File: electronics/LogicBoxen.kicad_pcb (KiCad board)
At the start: 2 copper layers, 50 x 35 mm, 47 parts, among them P1 Input, P2 Output, P3 Power, P4 L2, P5 L1, P6 OUT, Q1 Q_NMOS_DGS, SW1 DIPS_04, U1 4015, U2 4050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

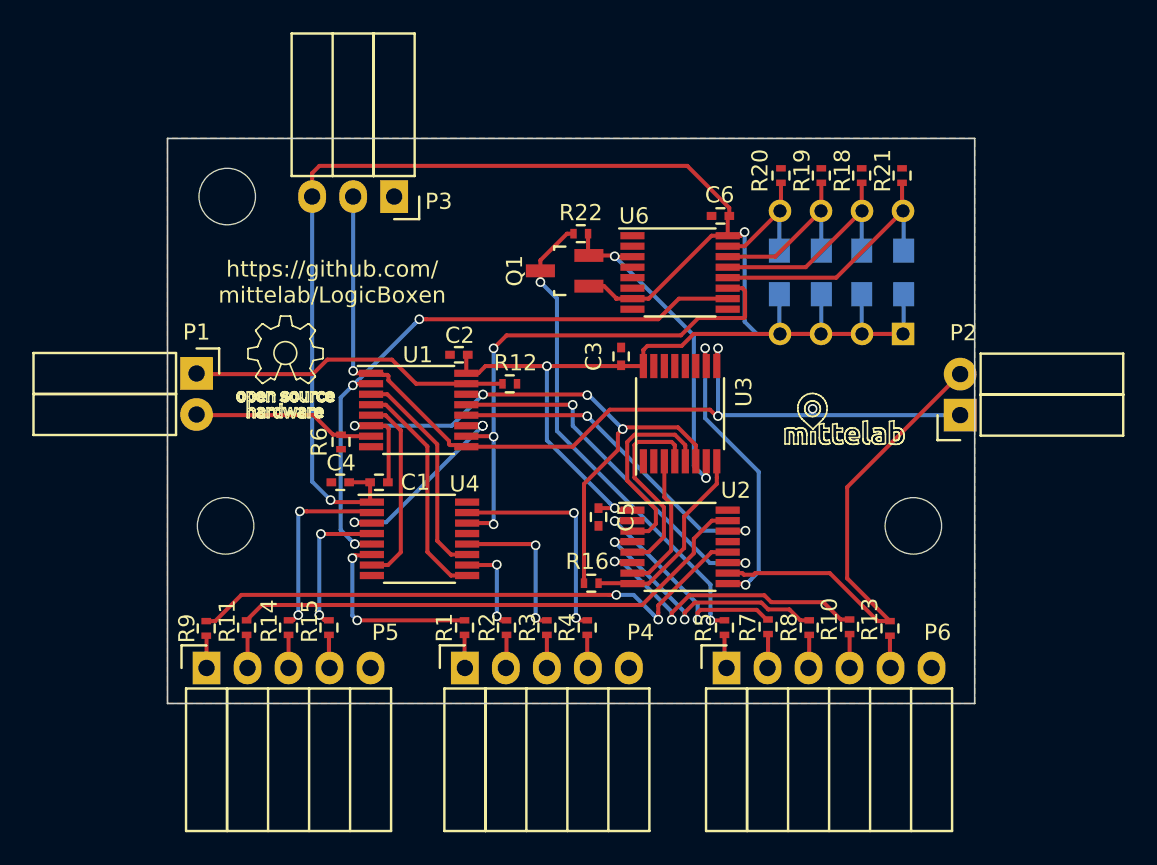
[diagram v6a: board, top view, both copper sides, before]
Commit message: Track shifting to match updated DRC rules
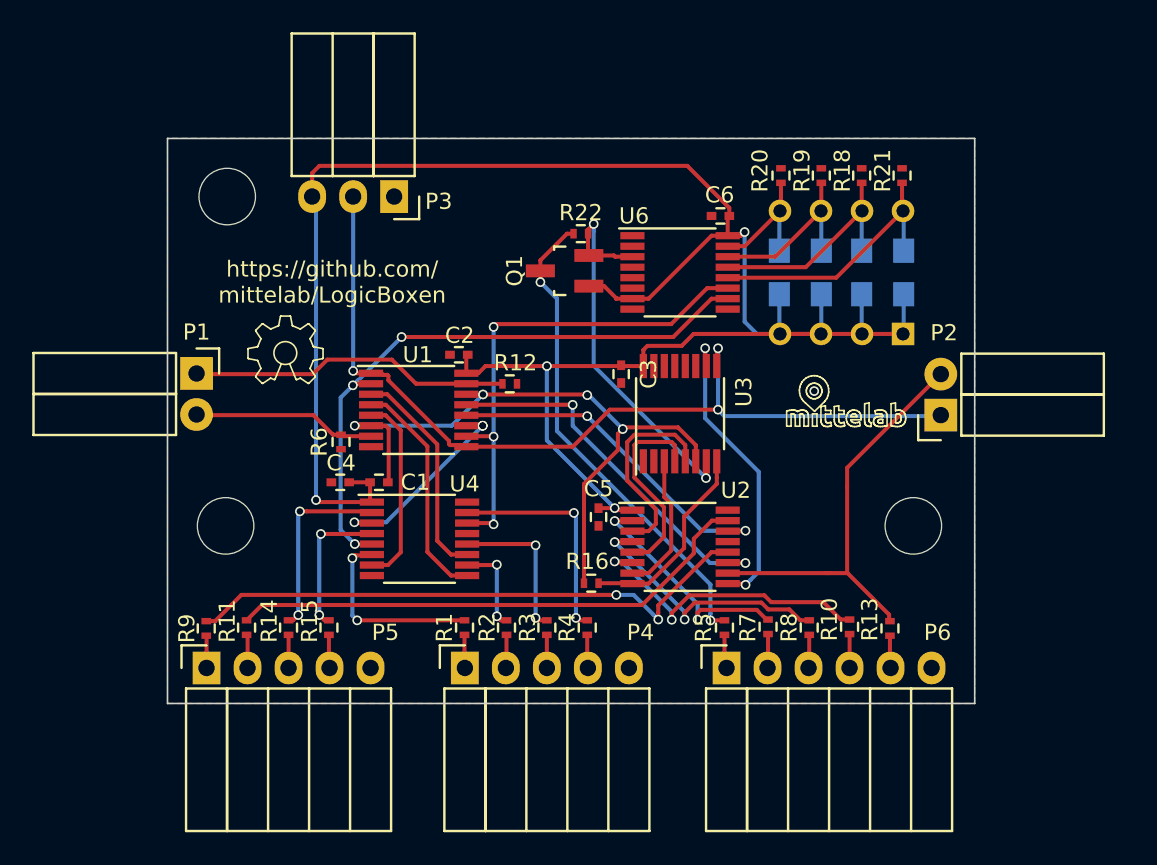
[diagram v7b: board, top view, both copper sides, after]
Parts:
- moved P2 1.20 mm to (71.9, 45.8)
- moved C3 1.10 mm to (52.1, 43.3), turned to 270 degrees
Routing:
- net Net-(P2-Pad2): track 30.7 -> 26.5 mm
- net /out: track 21.3 -> 24.6 mm
- net /in_a: track 33.4 -> 31.1 mm
- net /clock: track 57.6 -> 56.1 mm
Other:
- rule via_min_size: 0.3 -> 0.46

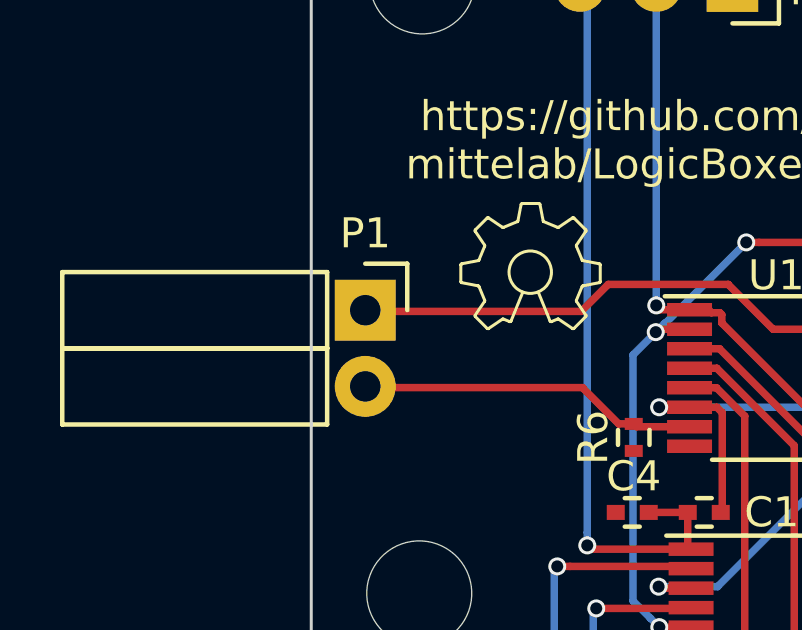
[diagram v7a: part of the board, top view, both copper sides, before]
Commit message: Move input connector away from edge
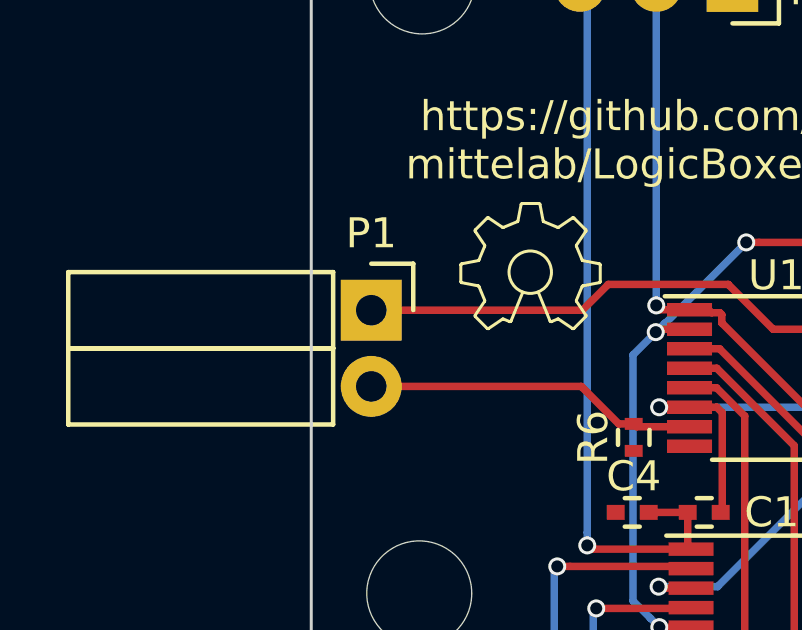
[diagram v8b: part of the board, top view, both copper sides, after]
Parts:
- moved P1 0.20 mm to (26.0, 43.3)
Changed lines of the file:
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@@
     (links 116)
     (no_connects 7)
-    (area 23.949999 28.649999 74.050001 63.750001)
+    (area 14.974999 18.25 91.1 72.325001)
     (thickness 1.6)
     (drawings 759)
@@
   )
   (module Socket_Strips:Socket_Strip_Angled_1x02 (layer F.Cu)
-    (at 25.8 43.26 270)
+    (at 26 43.26 270)
     (descr "Through hole socket strip")
     (tags "socket strip")
@@
   (via (at 43.544368 44.558738) (size 0.6) (drill 0.4) (layers F.Cu B.Cu) (net 1))
   (segment (start 49.8 56.25) (end 49.8 56.35) (width 0.25) (layer F.Cu) (net 1) (status 30))
+  (segment (start 33.9 42.4) (end 33.04 43.26) (width 0.25) (layer F.Cu) (net 2))
+  (segment (start 33.04 43.26) (end 26 43.26) (width 0.25) (layer F.Cu) (net 2))
   (segment (start 42.51 43.895) (end 44.695 43.895) (width 0.25) (layer F.Cu) (net 2) (status 30))
-  (segment (start 25.8 43.3) (end 33 43.3) (width 0.25) (layer F.Cu) (net 2))
-  (segment (start 33 43.3) (end 33.9 42.4) (width 0.25) (layer F.Cu) (net 2))
   (segment (start 33.9 42.4) (end 37.9 42.4) (width 0.25) (layer F.Cu) (net 2))
   (segment (start 39.395 43.895) (end 42.51 43.895) (width 0.25) (layer F.Cu) (net 2))
@@
   (segment (start 44.695 43.895) (end 44.8 44) (width 0.25) (layer F.Cu) (net 2) (status 30))
   (segment (start 34.75 47.05) (end 34.25 47.05) (width 0.25) (layer F.Cu) (net 3))
-  (segment (start 34.25 47.05) (end 33.04 45.84) (width 0.25) (layer F.Cu) (net 3))
-  (segment (start 33.04 45.84) (end 25.84 45.84) (width 0.25) (layer F.Cu) (net 3))
+  (segment (start 34.25 47.05) (end 33 45.8) (width 0.25) (layer F.Cu) (net 3))
+  (segment (start 33 45.8) (end 26 45.8) (width 0.25) (layer F.Cu) (net 3))
   (segment (start 25.84 45.84) (end 25.8 45.8) (width 0.25) (layer F.Cu) (net 3))
   (segment (start 36.61 47.145) (end 34.845 47.145) (width 0.25) (layer F.Cu) (net 3) (status 30))
